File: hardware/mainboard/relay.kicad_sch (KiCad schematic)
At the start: 6 parts, among them K1 RELAY, Q1 BC817

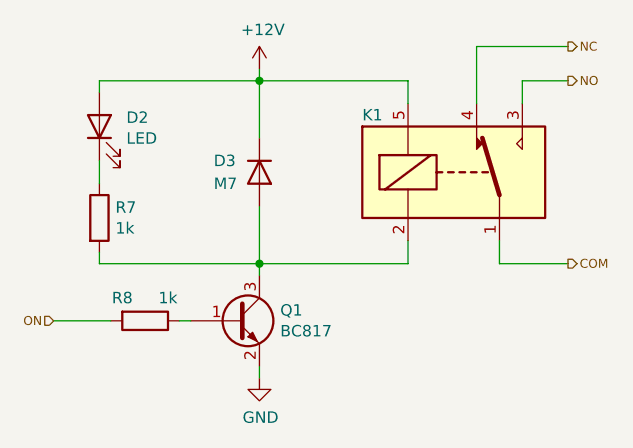
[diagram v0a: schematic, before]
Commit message: Mainboard routeado.
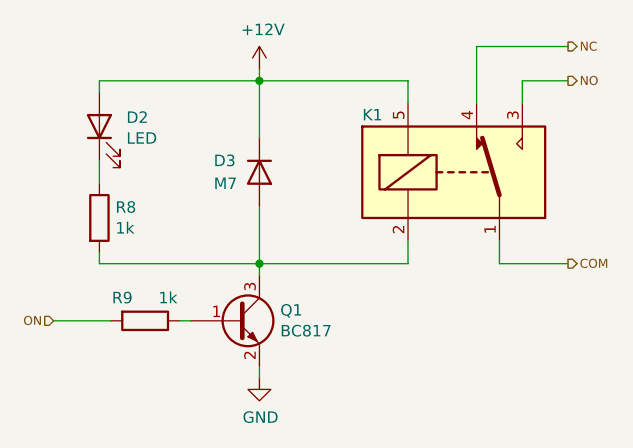
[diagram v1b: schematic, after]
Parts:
- renumbered R7 to R8, R8 to R9
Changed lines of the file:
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@@
   (symbol (lib_id "Device:R") (at 128.27 116.84 270) (unit 1)
     (in_bom yes) (on_board yes)
-    (property "Reference" "R8" (id 0) (at 125.73 114.3 90))
+    (property "Reference" "R9" (id 0) (at 125.73 114.3 90))
     (property "Value" "1k" (id 1) (at 130.81 114.3 90))
     (property "Footprint" "Resistor_SMD:R_1206_3216Metric" (id 2) (at 128.27 115.062 90)
@@
   (symbol (lib_id "Device:R") (at 123.19 105.41 0) (unit 1)
     (in_bom yes) (on_board yes)
-    (property "Reference" "R7" (id 0) (at 124.968 104.2416 0)
+    (property "Reference" "R8" (id 0) (at 124.968 104.2416 0)
       (effects (font (size 1.27 1.27)) (justify left))
     )
